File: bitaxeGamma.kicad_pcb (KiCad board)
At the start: 4 copper layers, 56.5 x 99.8 mm, 146 parts, among them J1 54-00164, J2 TC2030-IDC, J3 Conn_01x04, J4 Conn_01x06, J5 USB_C_Receptacle_USB2.0, J6 Conn_01x04, J7 Conn_01x04, SW1 GT-TC029B-H025-L1N, SW2 GT-TC029B-H025-L1N, T1 net-tie, U10 EMC2101, U2 TPS546D24ARVFR, U3 RT9080-33GJ5, U4 ESP32-S3-WROOM-1, U5 MCP1824T-1202E/OT, U6 MCP1824T-0802E, U7 25MHz, U8 BM1370_mode1, U9 SN74AVC4T774

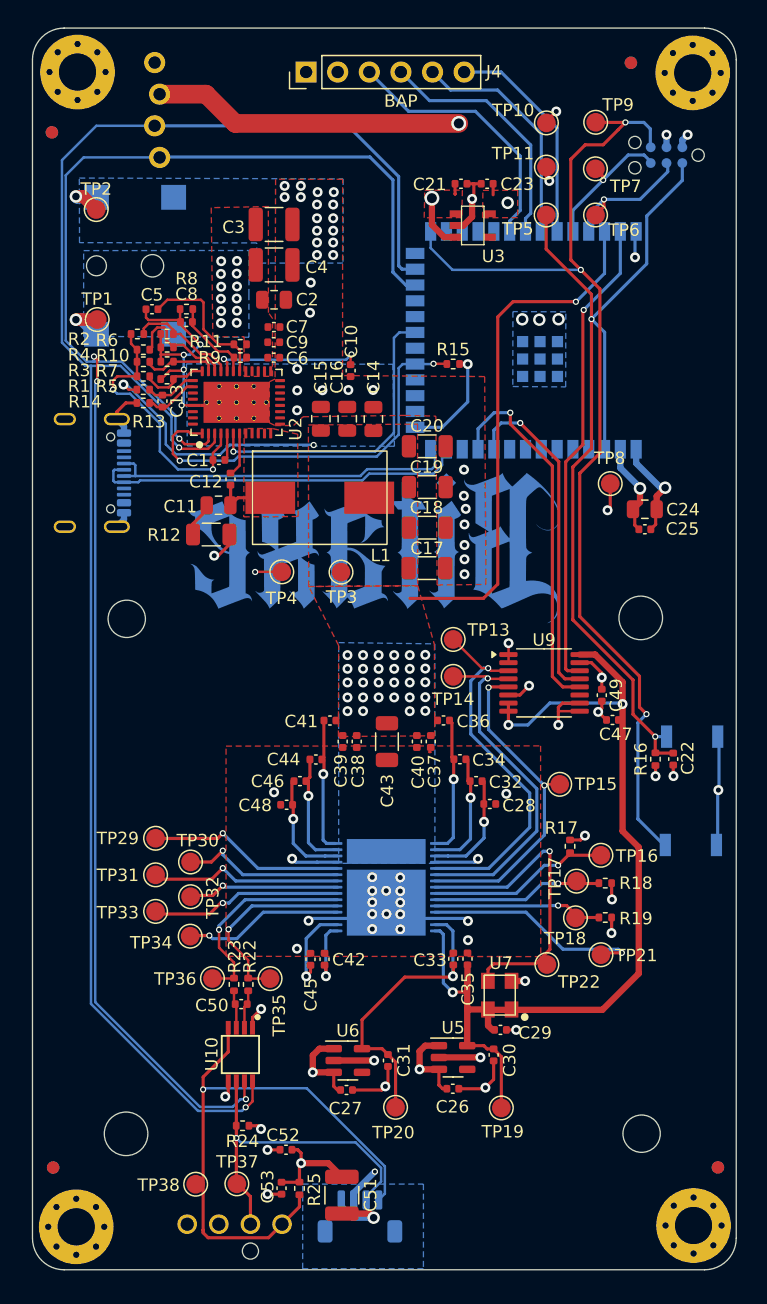
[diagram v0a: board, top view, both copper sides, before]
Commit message: barrel plug footprint, inductor footprint, asic footprint, gnd fill
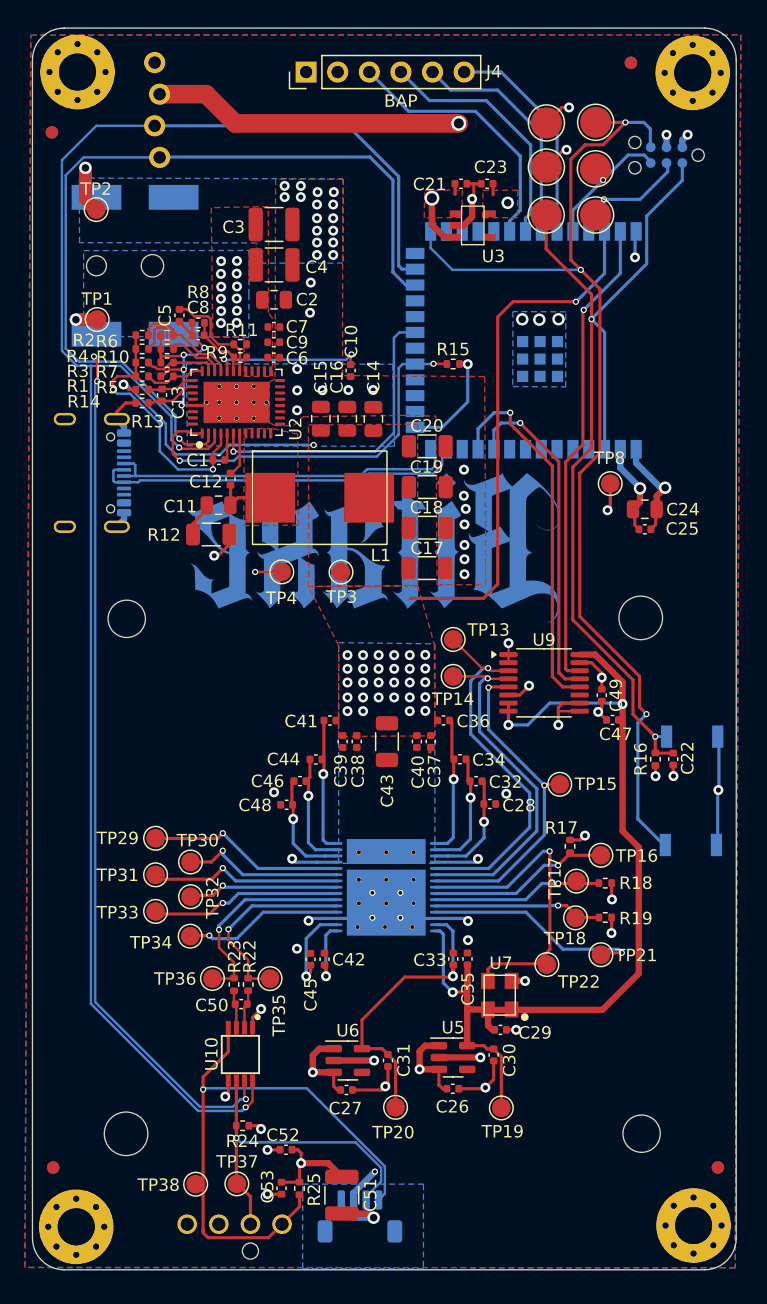
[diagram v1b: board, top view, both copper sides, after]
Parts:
- .: renamed from G***; value LOGO -> .
- TP10, TP11, TP5, TP6, TP7, TP9: footprint TestPoint:TestPoint_Pad_D1.5mm -> TestPoint:TestPoint_Pad_D2.5mm
- moved C5 2.26 mm to (89.0, 70.6), turned to 90 degrees
- moved R8 1.45 mm to (90.5, 71.2)
- moved C8 1.42 mm to (90.5, 72.2)
- moved C13 0.49 mm to (87.6, 77.0)
- moved R2 0.39 mm to (86.0, 72.2)
- moved R5 0.22 mm to (88.0, 75.5)
- moved R10 0.13 mm to (88.0, 73.3)
- moved R3 0.12 mm to (86.0, 74.4)
- moved R4 0.12 mm to (86.0, 73.3)
- moved R6 0.10 mm to (88.0, 72.2)
- moved R1 0.10 mm to (86.0, 75.5)
- moved R13 0.09 mm to (86.0, 77.6)
- moved R14 0.09 mm to (86.0, 76.6)
- moved R7 0.08 mm to (88.0, 74.4)
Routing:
- net /5V: track 199.0 -> 191.8 mm
- net GND: track 97.0 -> 100.7 mm, vias 81 -> 73
- net /Power/AGND: track 20.1 -> 17.1 mm
- net Net-(U2-AVIN): track 11.5 -> 8.73 mm
- net Net-(U2-EN/UVLO): track 6.88 -> 5.28 mm
- net /3V3: track 54.1 -> 55.1 mm
- net Net-(U2-MSEL1): track 5.45 -> 4.94 mm
- added copper zone on In2.Cu, net GND

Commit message: fix zones...
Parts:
- removed R2, R3, R4, R7: ~, Resistor_SMD:R_0402_1005Metric
- moved C5 1.73 mm to (90.7, 70.9), turned to 0 degrees
- moved R10 1.10 mm to (88.0, 74.4)
- moved R6 1.10 mm to (88.0, 73.3)
- moved C8 0.73 mm to (90.7, 72.9)
- moved R8 0.73 mm to (90.7, 71.9)
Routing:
- net Net-(U2-ADRSEL): track 5.87 -> 0.00 mm
- net Net-(U2-VSEL): track 9.06 -> 3.84 mm
- net /Power/AGND: track 17.1 -> 13.2 mm, vias 4 -> 3
- net Net-(U2-MSEL2): track 8.63 -> 4.86 mm
- net Net-(U2-BP1V5): track 21.1 -> 17.8 mm
- net Net-(U2-AVIN): track 8.73 -> 5.46 mm

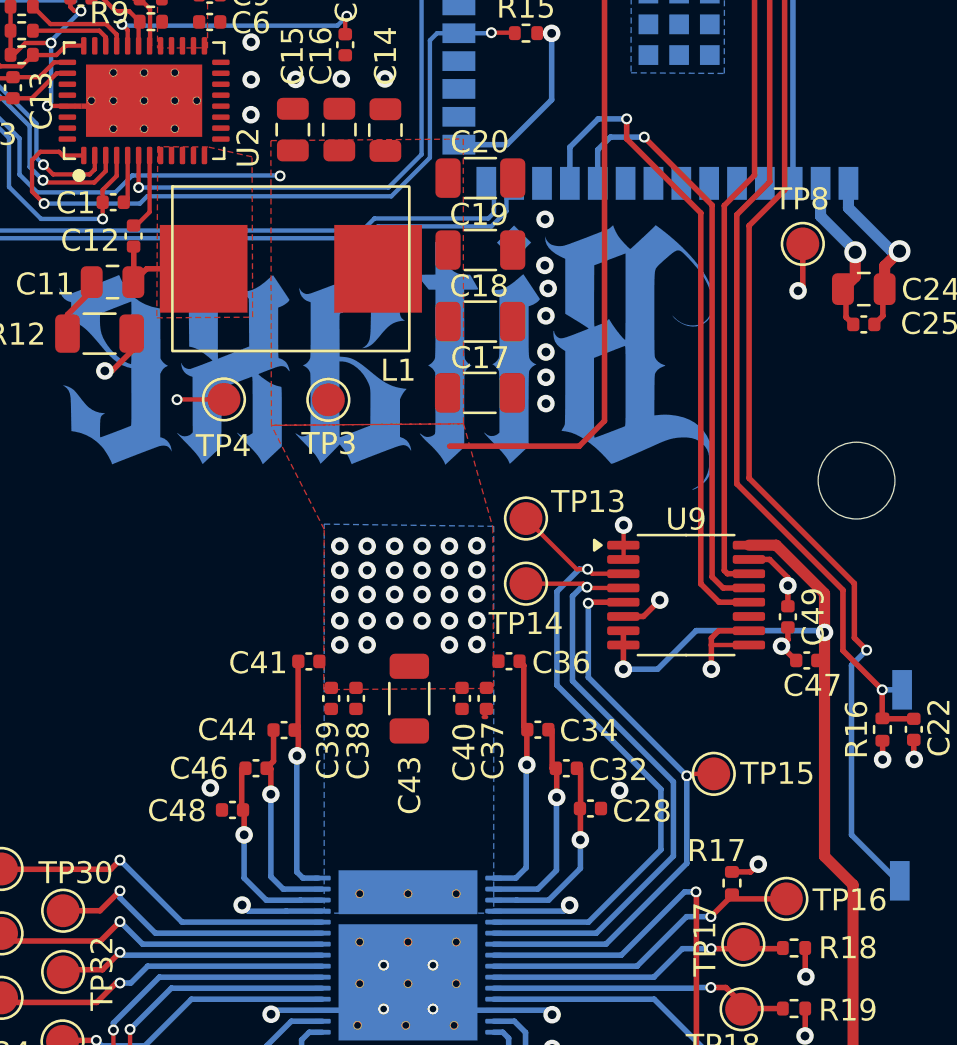
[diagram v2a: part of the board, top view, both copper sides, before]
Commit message: beefing up ASIC VDD width
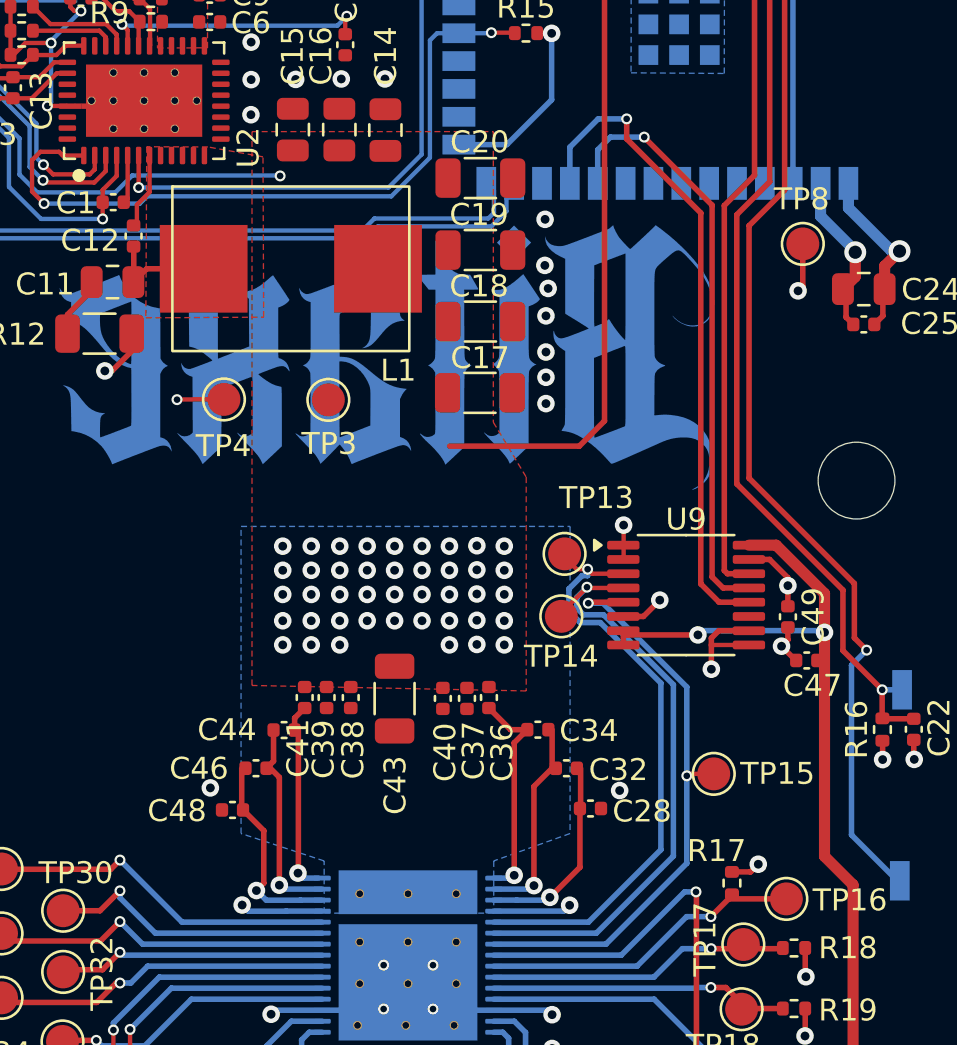
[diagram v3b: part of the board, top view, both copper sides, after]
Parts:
- moved TP13 2.39 mm to (112.8, 98.2)
- moved TP14 2.19 mm to (112.6, 101.1)
- moved C36 1.89 mm to (109.3, 104.8), turned to 90 degrees
- moved C41 1.66 mm to (100.9, 104.8), turned to -90 degrees
- moved C37 0.89 mm to (108.3, 104.8)
- moved C40 0.87 mm to (107.2, 104.8)
- moved C43 0.67 mm to (105.0, 104.8)
- moved C38 0.24 mm to (103.0, 104.8)
- moved C39 0.21 mm to (101.9, 104.8)
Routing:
- net /BM1370/RST_N: track 30.1 -> 27.8 mm
- net /BM1370/VDD1_1: track 10.8 -> 8.74 mm
- net /BM1370/1V2: track 77.1 -> 75.5 mm
- net /BM1370/VDD1_0: track 11.3 -> 10.0 mm
- net /BM1370/CI: track 28.7 -> 27.9 mm
- net /VDD: vias 31 -> 45

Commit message: DRC
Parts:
- moved TP14 4.05 mm to (115.2, 104.2)
- moved TP4 3.82 mm to (93.4, 91.2)
- moved TP13 2.79 mm to (114.4, 96.0)
- moved C14 2.32 mm to (106.9, 78.8)
- moved C16 2.32 mm to (104.8, 78.8)
- moved C15 2.24 mm to (102.6, 78.8)
- moved C18 1.62 mm to (110.5, 87.7)
- moved C19 1.62 mm to (110.5, 84.5)
- moved C20 1.62 mm to (110.5, 81.2)
- moved C17 1.62 mm to (110.5, 91.0)
- moved C41 1.00 mm to (99.9, 104.8)
- moved C36 0.70 mm to (110.0, 104.8)
- moved C43 0.40 mm to (105.4, 104.8)
- moved C6 0.33 mm to (96.9, 74.0)
- moved C9 0.33 mm to (96.9, 72.8)
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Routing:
- net /RX: track 29.9 -> 34.9 mm
- net /TX: track 27.1 -> 31.2 mm
- net /BM1370/RO: track 27.4 -> 25.5 mm
- net /BM1370/CI: track 27.9 -> 29.6 mm
- net /VDD: track 62.5 -> 60.8 mm, vias 45 -> 63
- net /BM1370/0V8: track 24.0 -> 22.9 mm
- net /BM1370/VDD1_0: track 10.0 -> 9.32 mm
- net Net-(U2-AVIN): track 5.46 -> 5.97 mm
- net /3V3: track 55.1 -> 55.5 mm, vias 11 -> 12
- net GND: track 100.6 -> 100.4 mm, vias 73 -> 84
